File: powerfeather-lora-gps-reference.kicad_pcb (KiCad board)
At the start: 2 copper layers, 23 x 58 mm, 18 parts, among them J1 Conn_01x05, J11 Conn_01x04, J2 Conn_01x02, J3 Conn_01x04, J4 Conn_01x02, J5 Conn_01x02, J6 Conn_01x04, J7 Conn_01x04, J8 Conn_01x03, J9 Conn_01x03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

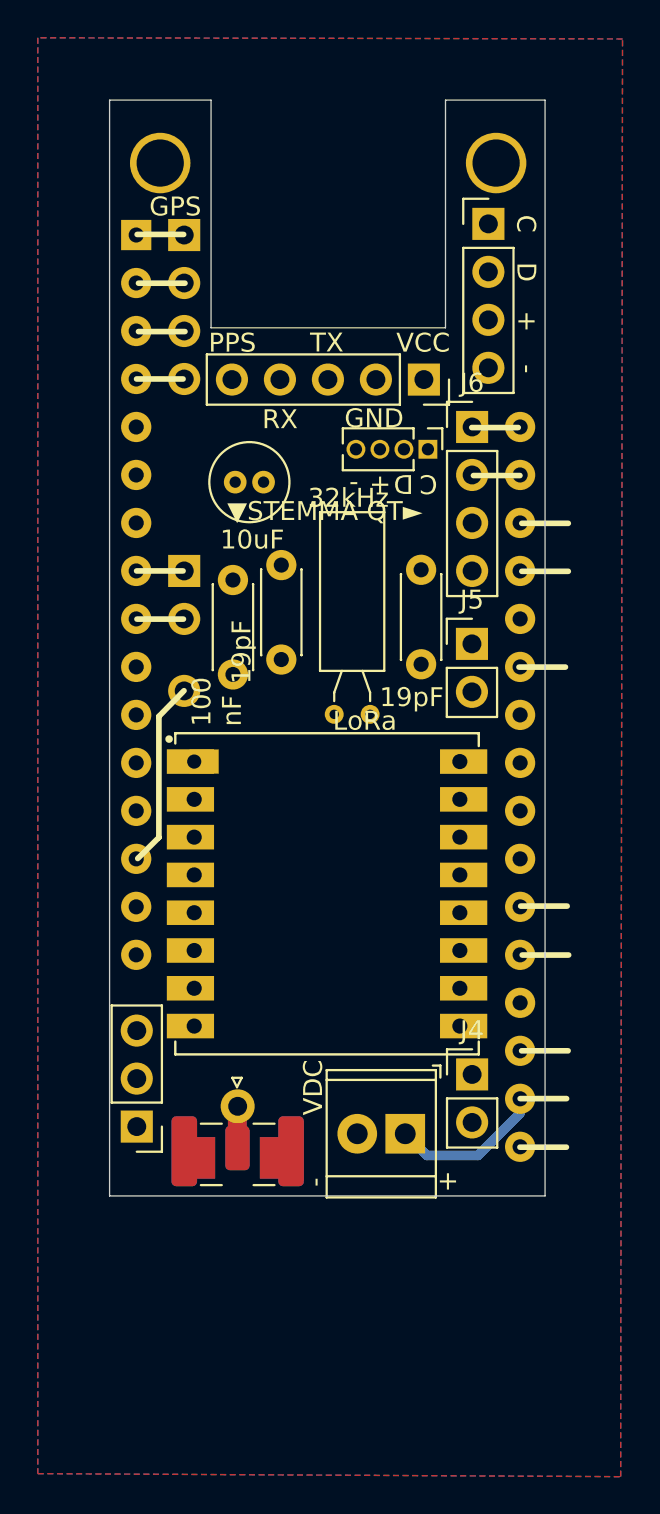
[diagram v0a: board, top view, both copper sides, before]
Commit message: Resetting some components for layout
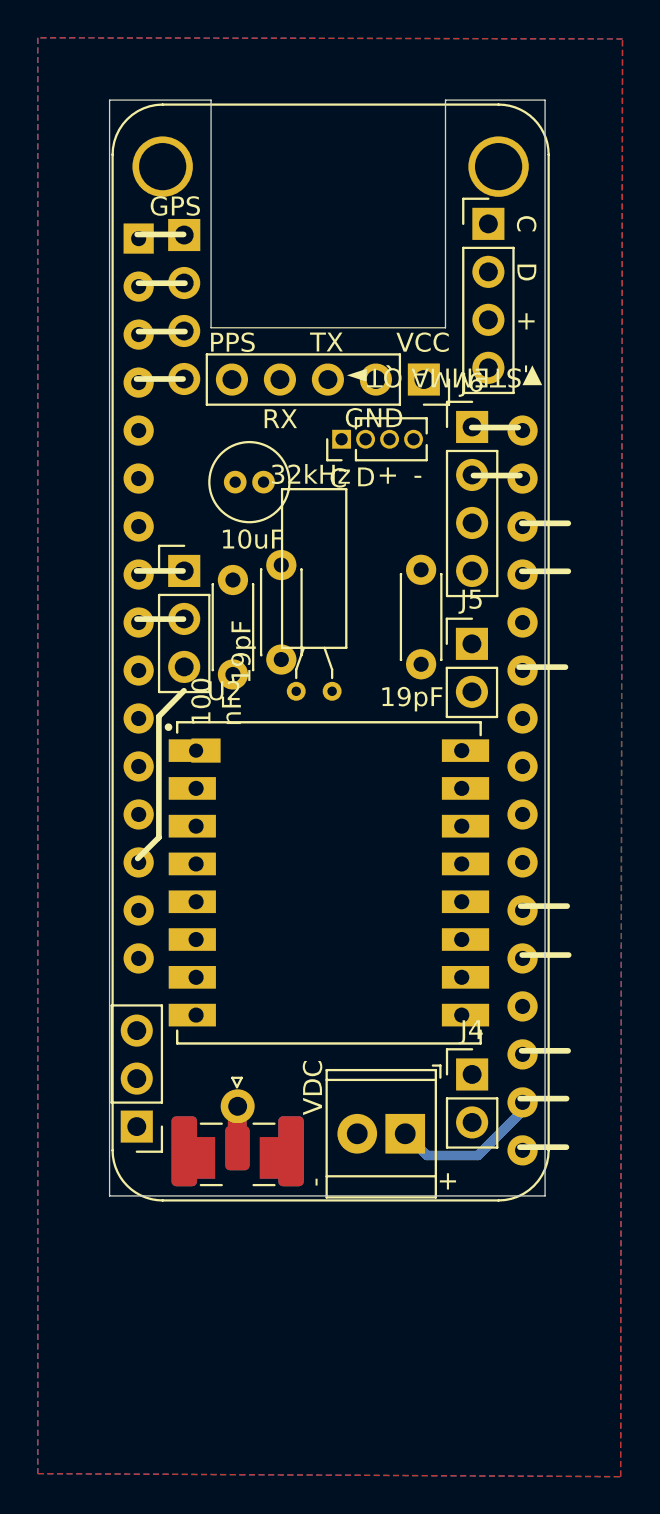
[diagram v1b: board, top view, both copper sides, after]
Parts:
- removed U1: RA-01H, PowerFeather_LoRa:Lora126x
- added U2: Lora126x, PowerFeather_LoRa_GPS:Lora126x, F.Cu at (131.2, 110.9)
- A1: footprint PowerFeather:PowerFeather_Wing1 -> PowerFeather_KiCAD_Lib:PowerFeather_Mainboard
- moved J7 4.60 mm to (131.8, 87.5), turned to 90 degrees
- moved Y1 2.35 mm to (131.3, 100.8)
- moved A1 0.23 mm to (121.1, 76.8)

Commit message: Rearrange rough layout again
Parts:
- added J10: Conn_01x01, Connector_PinHeader_2.54mm:PinHeader_1x01_P2.54mm_Vertical, F.Cu at (140.0, 76.5)
- J3: footprint Connector_PinHeader_2.54mm:PinHeader_1x04_P2.54mm_Vertical -> Connector_PinHeader_1.27mm:PinHeader_1x04_P1.27mm_Vertical
- moved J7 12.7 mm to (141.1, 78.8), turned to 0 degrees
- moved J3 2.80 mm to (139.0, 78.8)
- moved C1 2.22 mm to (136.1, 97.1)
- moved Y1 2.10 mm to (133.4, 100.7)
- moved C2 1.97 mm to (128.8, 97.2)
- moved C4 1.64 mm to (125.2, 91.0), turned to 90 degrees
- moved C3 0.79 mm to (126.2, 95.7)
- moved A1 0.22 mm to (121.0, 76.7)
- moved J2 0.21 mm to (135.2, 124.0)
- moved J9 0.07 mm to (121.1, 123.8)
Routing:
- net Net-(AE1-A): track 0.00 -> 14.9 mm
- net /SCL: track 0.00 -> 12.5 mm
- net /RXD0: track 0.00 -> 10.0 mm
- net /SDA: track 0.00 -> 7.38 mm
- net /D7: track 0.00 -> 4.84 mm
- net /TXD0: track 0.00 -> 4.01 mm
- net /D11: track 0.00 -> 3.19 mm
- net VS: track 0.00 -> 2.55 mm
- net /D13: track 0.00 -> 2.55 mm
- net +BATT: track 0.00 -> 2.55 mm
- net /EN: track 0.00 -> 2.55 mm
- net /SCL1: track 0.00 -> 2.11 mm
- net GND: track 0.00 -> 2.11 mm
- net /SDA1: track 0.00 -> 2.11 mm
- net +3.3VP: track 0.00 -> 2.11 mm
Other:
- board size 23 x 58 mm -> 23.1 x 58.1 mm

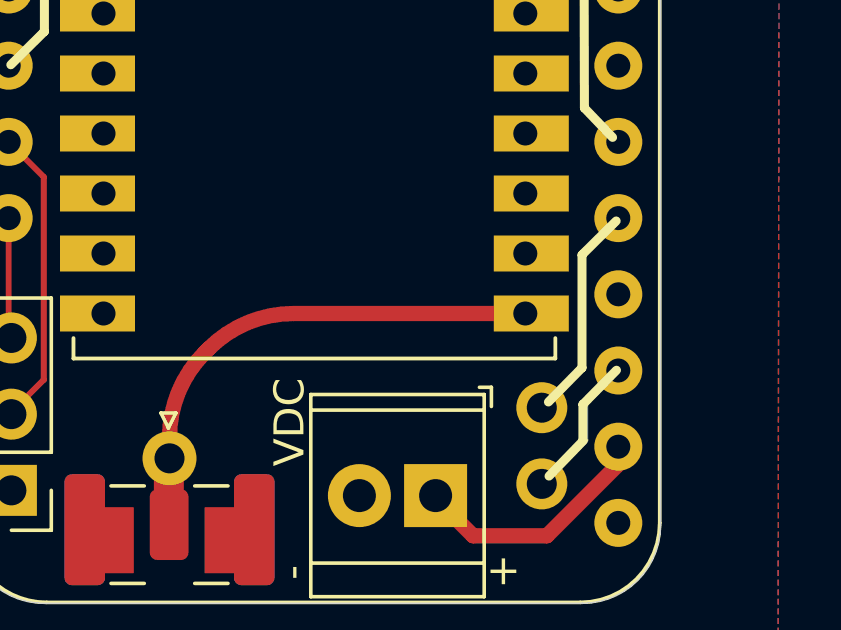
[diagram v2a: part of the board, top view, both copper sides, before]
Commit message: Add antenna marker
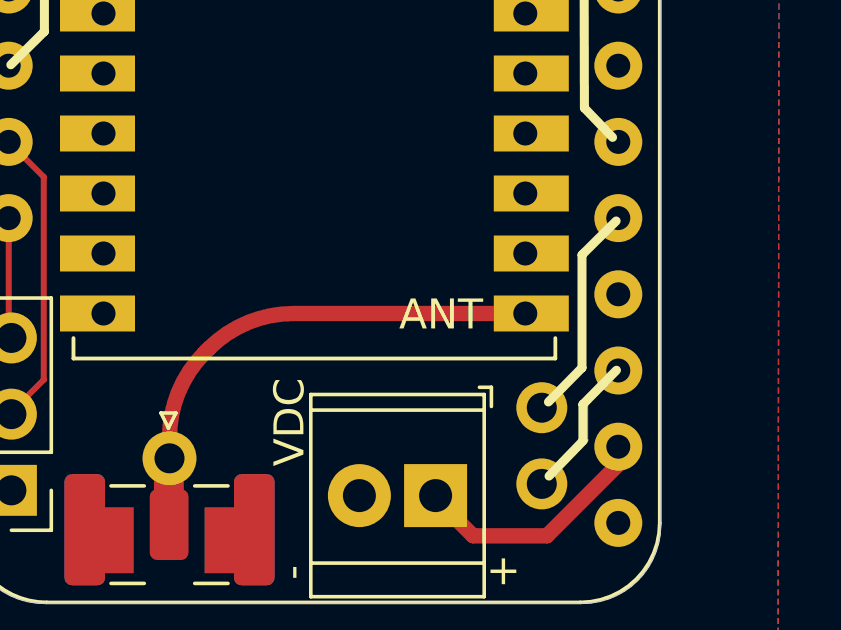
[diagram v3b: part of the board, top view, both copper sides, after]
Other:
- board text added: "ANT"
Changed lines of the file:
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@@
 		(fp_arc
 			(start 1.27 50.910002)
-			(mid -0.603834 50.133835)
+			(mid -0.603834 50.133836)
 			(end -1.38 48.260002)
 			(stroke
@@
 		(layer "F.Fab")
 	)
+	(gr_text "ANT"
+		(at 133.98 118.55 0)
+		(layer "F.SilkS")
+		(effects
+			(font
+				(size 1 1)
+				(thickness 0.15)
+			)
+			(justify left bottom)
+		)
+	)
 	(segment

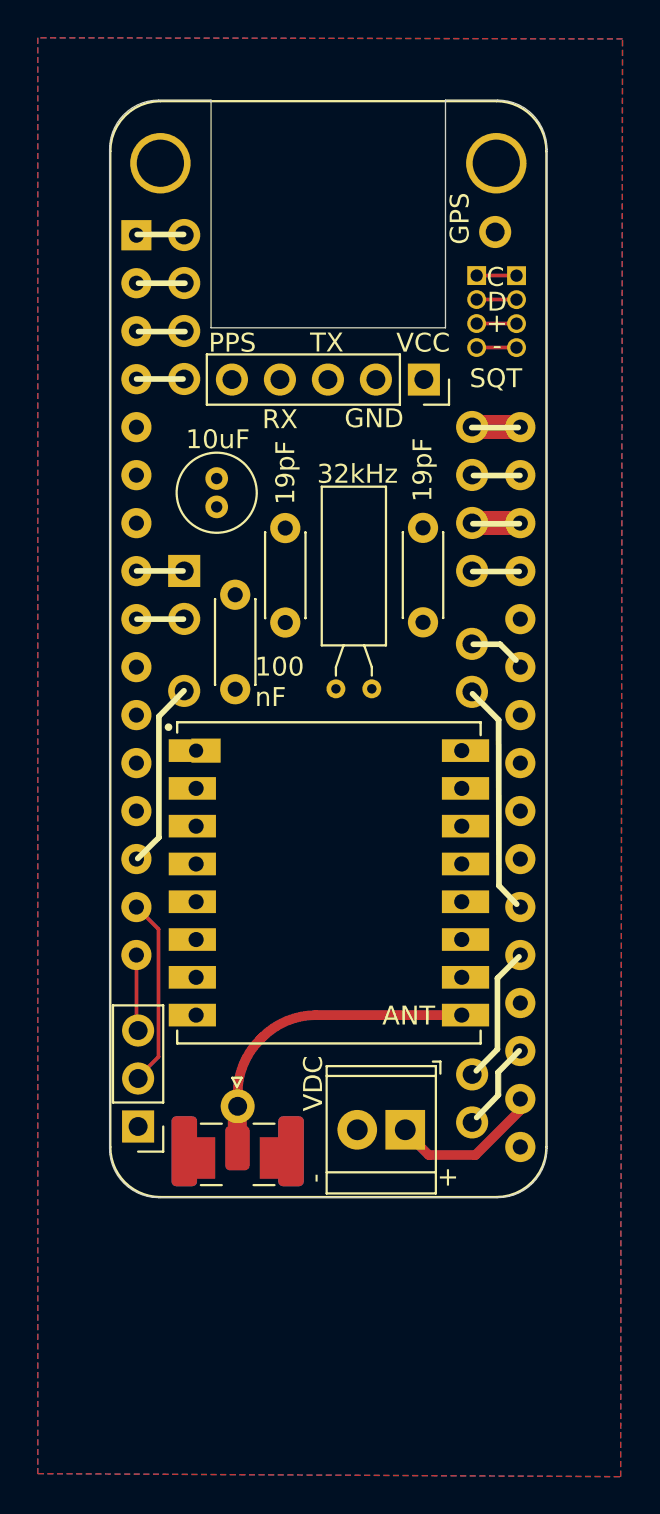
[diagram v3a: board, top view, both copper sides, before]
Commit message: Reroute traces
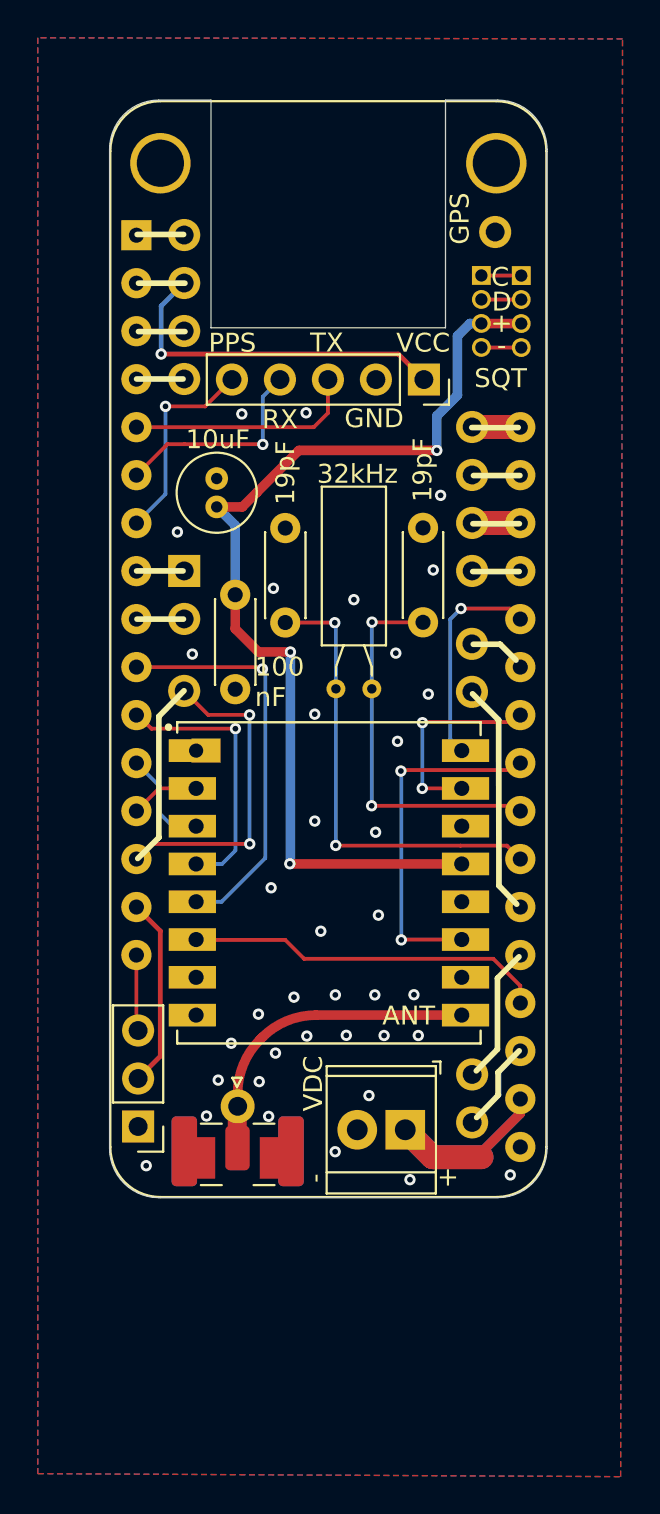
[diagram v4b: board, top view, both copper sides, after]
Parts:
- AE1: footprint PowerFeather_LoRa:SMA_Edge -> PowerFeather_LoRa_GPS:SMA_Edge
- moved J7 0.25 mm to (141.3, 78.8)
- moved J3 0.25 mm to (139.2, 78.8)
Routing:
- net +3.3VP: track 2.11 -> 53.5 mm, vias 0 -> 3
- net Net-(A1-D5): track 0.00 -> 24.5 mm, vias 0 -> 2
- net /LORA_CS: track 0.00 -> 21.4 mm, vias 0 -> 1
- net +3.3V: track 0.00 -> 21.3 mm, vias 0 -> 1
- net Net-(A1-D6): track 0.00 -> 20.6 mm, vias 0 -> 2
- net /LORA_RST: track 0.00 -> 19.1 mm
- net /LORA_DIO3: track 0.00 -> 18.7 mm, vias 0 -> 2
- net /RX: track 0.00 -> 17.2 mm, vias 0 -> 2
- net /LORA_SCK: track 0.00 -> 14.4 mm, vias 0 -> 1
- net /GPS_TX: track 0.00 -> 12.2 mm
- net /LORA_BUSY: track 0.00 -> 11.4 mm, vias 0 -> 1
- net /GPS_RX: track 0.00 -> 11.2 mm, vias 0 -> 1
- net /GPS_PPS: track 0.00 -> 10.9 mm, vias 0 -> 1
- net /LORA_DIO1: track 0.00 -> 10.9 mm, vias 0 -> 2
- net VDC: track 8.18 -> 17.1 mm
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
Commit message: Fix some silkscreen
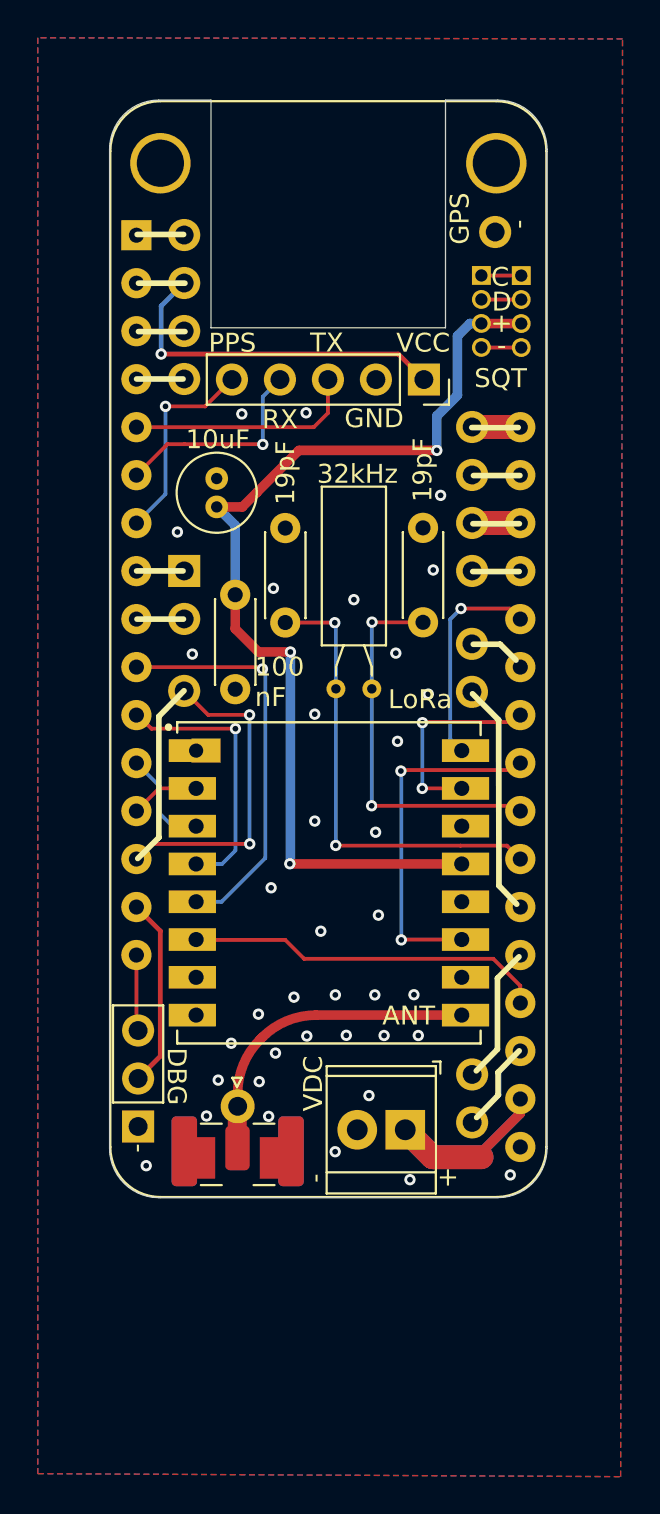
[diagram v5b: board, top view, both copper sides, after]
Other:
- board text added: "-"
- board text added: "DBG"
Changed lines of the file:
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@@
 			)
 		)
+		(property "Silkscreen" "LoRa"
+			(at 4.83 -9.71 0)
+			(unlocked yes)
+			(layer "F.SilkS")
+			(effects
+				(font
+					(size 1 1)
+					(thickness 0.15)
+				)
+			)
+		)
 		(sheetname "Root")
 		(sheetfile "powerfeather-lora-gps-reference.kicad_sch")
@@
 		)
 		(fp_line
-			(start -1.33 0)
-			(end -1.33 -1.33)
-			(stroke
-				(width 0.12)
-				(type solid)
-			)
-			(layer "F.SilkS")
-		)
-		(fp_line
-			(start -1.33 -1.33)
-			(end 0 -1.33)
-			(stroke
-				(width 0.12)
-				(type solid)
-			)
-			(layer "F.SilkS")
-		)
-		(fp_line
 			(start 1.27 6.35)
 			(end -1.27 6.35)
@@
 		(layer "F.Fab")
 	)
+	(gr_text "DBG"
+		(at 122.51 119.64 270)
+		(layer "F.SilkS")
+		(effects
+			(font
+				(size 1 1)
+				(thickness 0.15)
+			)
+			(justify left bottom)
+		)
+	)
+	(gr_text "-"
+		(at 140.78 75.82 270)
+		(layer "F.SilkS")
+		(effects
+			(font
+				(size 1 1)
+				(thickness 0.15)
+			)
+			(justify left bottom)
+		)
+	)
 	(gr_text "ANT"
 		(at 133.98 118.55 0)
 		(layer "F.SilkS")
 		(effects
+			(font
+				(size 1 1)
+				(thickness 0.15)
+			)
+			(justify left bottom)
+		)
+	)
+	(gr_text "-"
+		(at 120.55 124.72 -90)
+		(layer "F.SilkS")
+		(effects

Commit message: Mark main pins in silkscreen
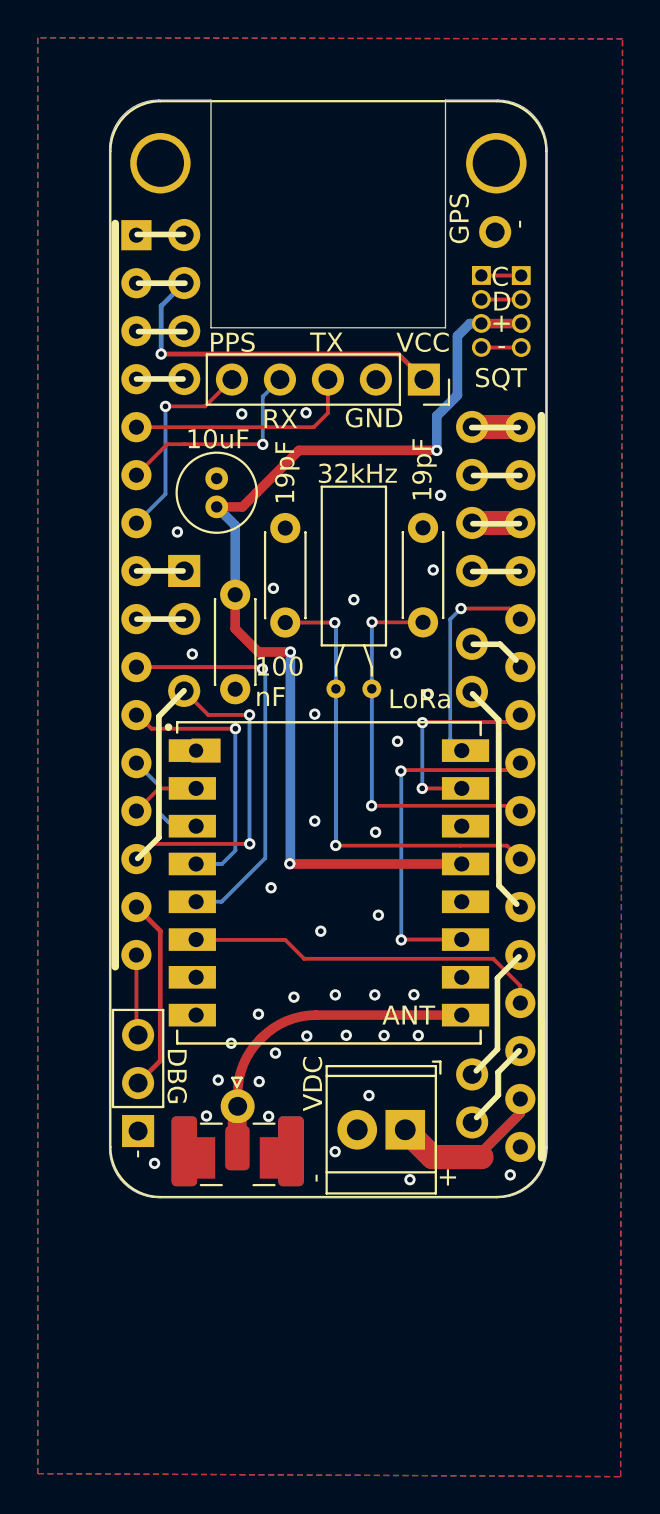
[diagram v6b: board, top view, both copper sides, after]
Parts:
- moved J9 0.24 mm to (121.1, 124.1)
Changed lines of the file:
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@@
 	(footprint "Connector_PinHeader_2.54mm:PinHeader_1x03_P2.54mm_Vertical"
 		(layer "F.Cu")
-		(at 121.06 123.825 180)
+		(at 121.06 124.065 180)
 		(descr "Through hole straight pin header, 1x03, 2.54mm pitch, single row")
 		(tags "Through hole pin header THT 1x03 2.54mm single row")
@@
 	)
 	(gr_line
+		(start 119.85 76.03)
+		(end 119.85 115.37)
+		(stroke
+			(width 0.4)
+			(type default)
+		)
+		(layer "F.SilkS")
+	)
+	(gr_line
 		(start 138.76 100.92)
 		(end 140.14 102.31)
@@
 	)
 	(gr_line
+		(start 142.41 86.2)
+		(end 142.42 125.48)
+		(stroke
+			(width 0.4)
+			(type default)
+		)
+		(layer "F.SilkS")
+	)
+	(gr_line
 		(start 120.98 94.42)
 		(end 123.44 94.42)
@@
 	)
 	(gr_text "-"
-		(at 120.55 124.72 -90)
+		(at 120.56 125.03 -90)
 		(layer "F.SilkS")
 		(effects
@@
 	)
 	(via
-		(at 121.49 125.9)
+		(at 121.93 125.78)
 		(size 0.6)
 		(drill 0.3)
@@
 	(segment
 		(start 120.97 114.75)
-		(end 120.97 118.73)
+		(end 120.97 118.895)
+		(width 0.2)
+		(layer "F.Cu")
+		(net 27)
+	)
+	(segment
+		(start 120.97 118.895)
+		(end 121.06 118.985)
 		(width 0.2)
 		(layer "F.Cu")
@@
 	)
 	(segment
-		(start 120.97 112.21)
-		(end 122.237 113.477)
+		(start 122.237 113.477)
+		(end 122.237 120.348)
 		(width 0.254)
 		(layer "F.Cu")
@@
 	)
 	(segment
-		(start 122.237 113.477)
-		(end 122.237 120.108)
+		(start 120.97 112.21)
+		(end 122.237 113.477)
 		(width 0.254)
 		(layer "F.Cu")
@@
 	)
 	(segment
-		(start 122.237 120.108)
-		(end 121.06 121.285)
+		(start 122.237 120.348)
+		(end 121.06 121.525)
 		(width 0.254)
 		(layer "F.Cu")
